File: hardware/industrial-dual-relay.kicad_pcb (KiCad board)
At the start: 2 copper layers, 40 x 40 mm, 34 parts, among them P1 CON-SENSOR2, P2 BOOT, P3 CONN_8, P4 Debug, Q2 G5Q-1, Q3 G5Q-1, U1 XMC1100, U4 DRILL, U5 DRILL, U6 DRILL

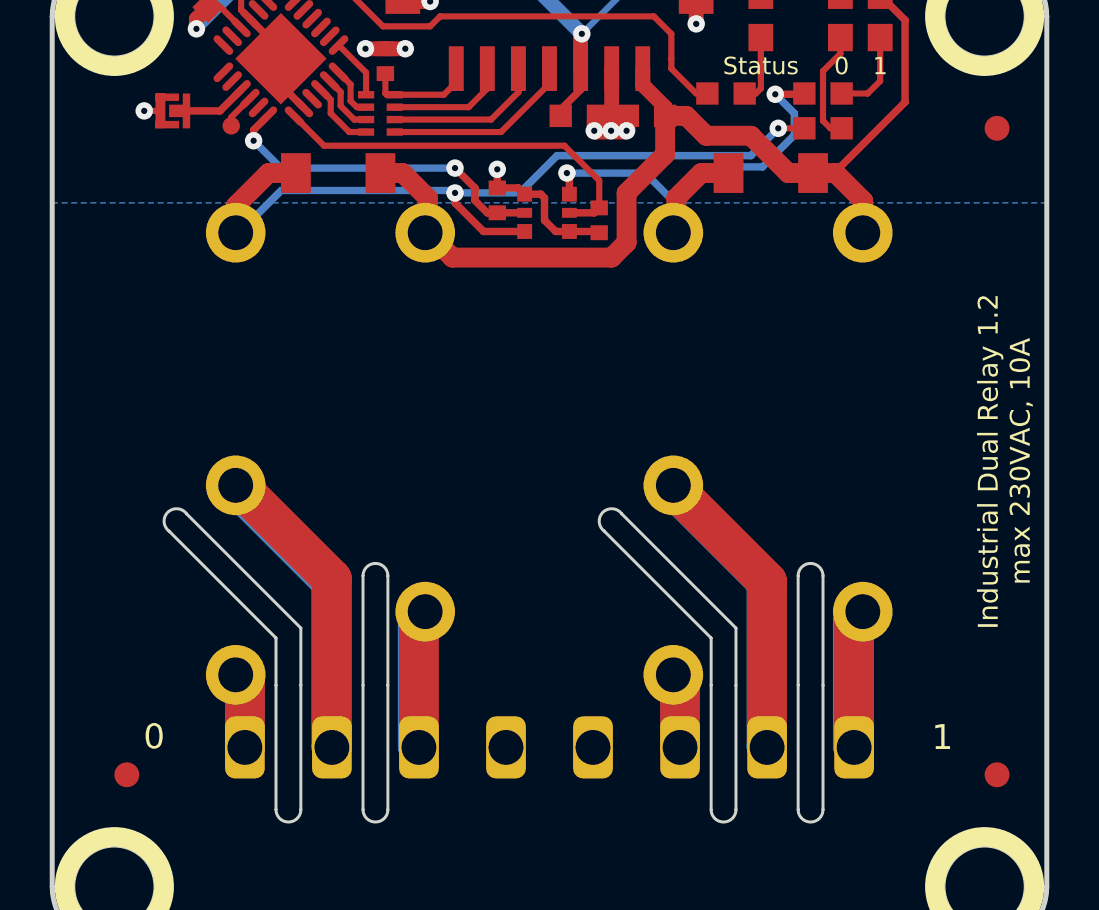
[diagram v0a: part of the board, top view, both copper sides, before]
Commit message: Version 1.3: changed just F.Silkscreen! added Pin description NO COM NC on F.Silkscreen
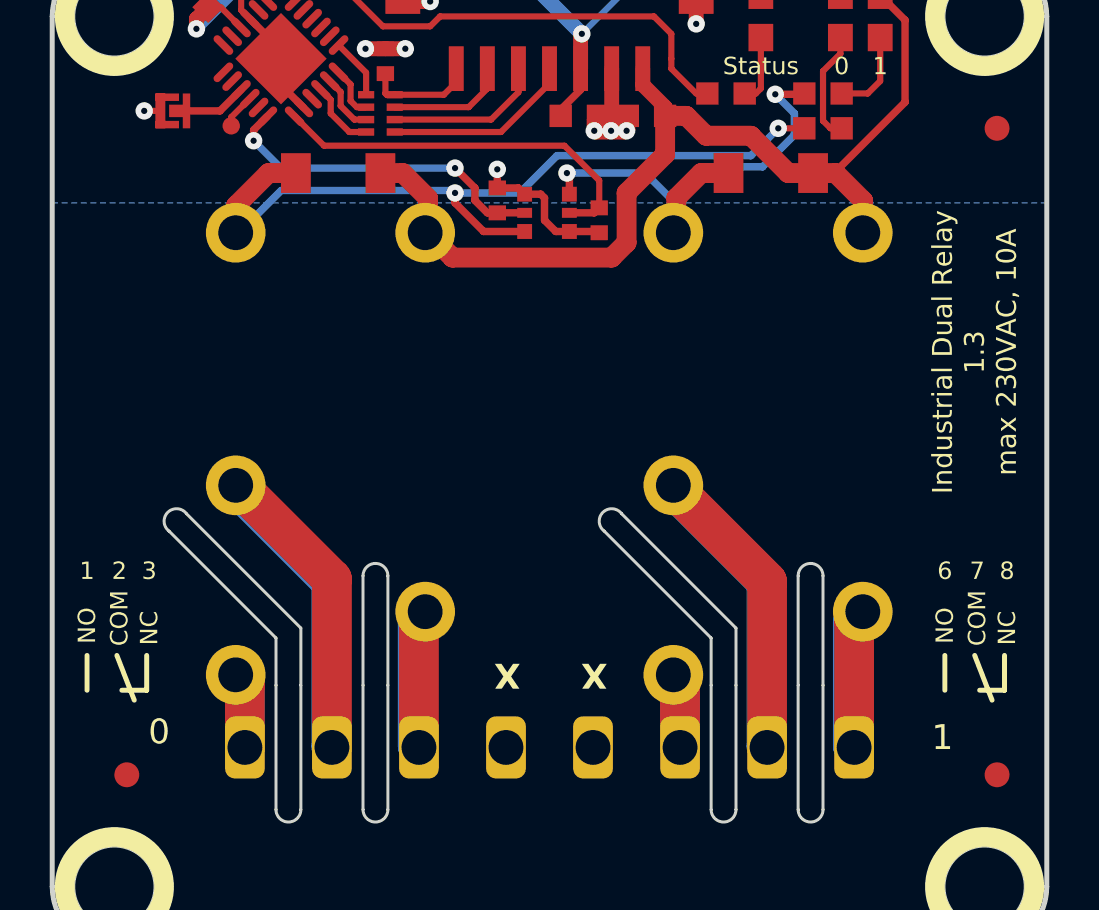
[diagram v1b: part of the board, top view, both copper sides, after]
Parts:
- renumbered locked to Q1
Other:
- board text added: "2"
- board text added: "3"
- board text added: "6"
- board text added: "7"
- board text added: "8"
- board text added: "Industrial Dual Relay 1.3 max 230VAC, 10A"
- board text removed: "Industrial Dual Relay 1.2 max 230VAC, 10A"

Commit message: final version 1.3: diff 1.2 changed silkscreen
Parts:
- removed REF**: DRILL_NP_New, kicad-libraries:DRILL_NP
- added U7: DRILL, kicad-libraries:DRILL_NP, F.Cu at (134.3, 86.4)
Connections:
- Q1 pad 2: RELAY1 -> RELAY0
- Q1 pad 5: RELAY0 -> RELAY1
- R4 pad 2: RELAY1 -> RELAY0
- R5 pad 2: RELAY0 -> RELAY1
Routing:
- net RELAY1: track 15.7 -> 13.6 mm, vias 0 -> 2
- net RELAY0: track 13.6 -> 15.7 mm, vias 2 -> 0

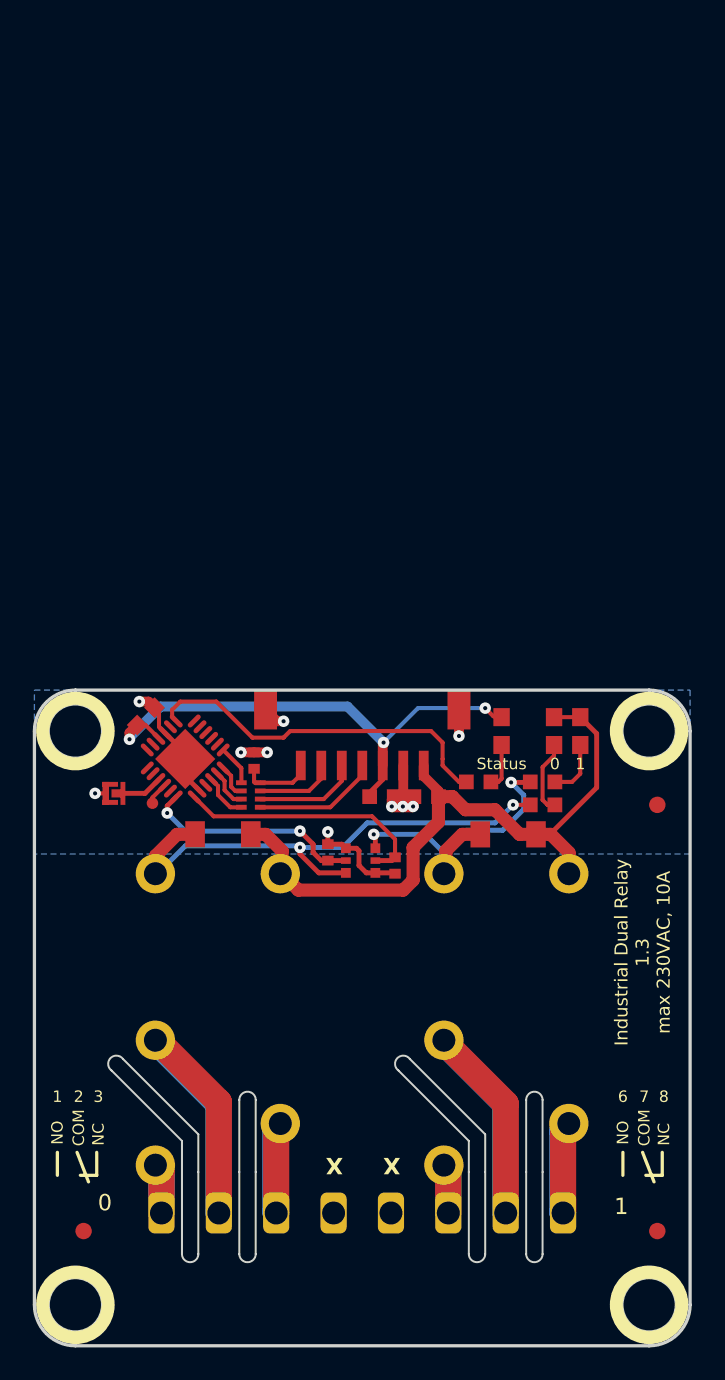
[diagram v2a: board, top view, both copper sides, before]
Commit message: version 1.3: fix dates and pcb rotation
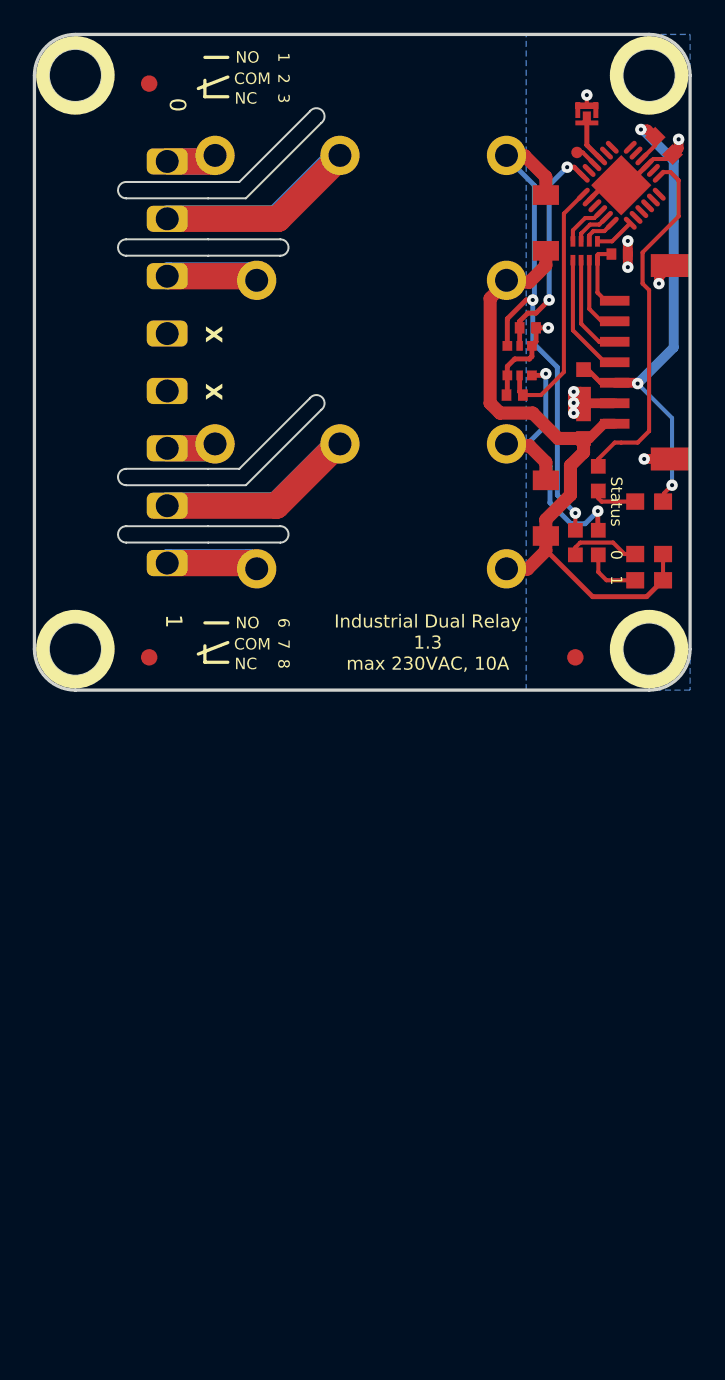
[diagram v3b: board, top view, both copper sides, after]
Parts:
- moved U6 75.0 mm to (134.3, 46.4), turned to 0 degrees
- moved Fiducial_Mark 70.1 mm to (138.8, 46.9), turned to 0 degrees
- moved P3 53.2 mm to (139.9, 63.9), turned to -90 degrees
- moved U5 53.2 mm to (134.3, 81.4), turned to 0 degrees
- moved U7 53.2 mm to (169.3, 46.4), turned to -90 degrees
- moved P2 50.5 mm to (165.5, 48.8), turned to -90 degrees
- moved P4 47.4 mm to (164.9, 51.1), turned to 0 degrees
- moved C4 47.0 mm to (170.2, 50.7), turned to -45 degrees
- moved Fiducial_Mark 46.8 mm to (138.8, 81.9), turned to 0 degrees
- moved VAL 45.9 mm to (156.2, 55.4), turned to 90 degrees
- moved U1 44.0 mm to (167.6, 53.1), turned to 135 degrees
- moved D4 42.2 mm to (163.0, 55.4), turned to 90 degrees
- moved RP1 39.0 mm to (165.4, 57.1), turned to 0 degrees
- moved Q2 38.7 mm to (160.6, 58.9), turned to 0 degrees
- moved C2 38.1 mm to (167.5, 57.3), turned to 180 degrees
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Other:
- outline, holes or cut-outs redrawn
- board text added: "Copyright Tinkerforge GmbH 2026. This documentation describes Open Hardware and is licensed under the CERN OHL v. 1.1. You may redistribute and modify this documentation under the terms of the CERN OHL v.1.1. (http://ohwr.org/cernohl). This documentation is distributed WITHOUT ANY EXPRESS OR IMPLIED WARRANTY, INCLUDING OF MERCHANTABILITY, SATISFACTORY QUALITY AND FITNESS FOR A PARTICULAR PURPOSE.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"
- board text removed: "Copyright Tinkerforge GmbH 2023. This documentation describes Open Hardware and is licensed under the CERN OHL v. 1.1. You may redistribute and modify this documentation under the terms of the CERN OHL v.1.1. (http://ohwr.org/cernohl). This documentation is distributed WITHOUT ANY EXPRESS OR IMPLIED WARRANTY, INCLUDING OF MERCHANTABILITY, SATISFACTORY QUALITY AND FITNESS FOR A PARTICULAR PURPOSE.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"
